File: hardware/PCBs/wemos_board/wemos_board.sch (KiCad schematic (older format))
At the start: 6 parts, among them J1 USB, J2 Servo, U1 WeMos_D1_mini

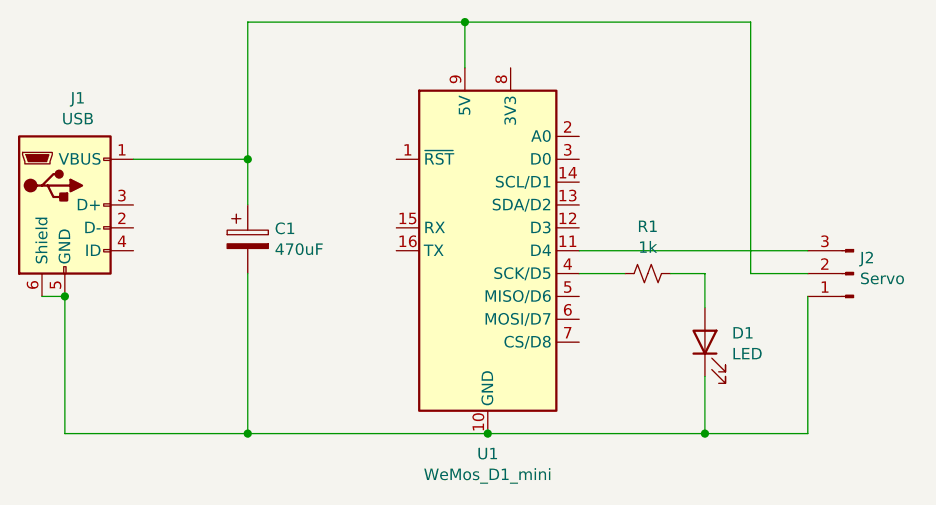
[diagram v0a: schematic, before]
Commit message: fix: wemos_board fix footprints and added rst control line
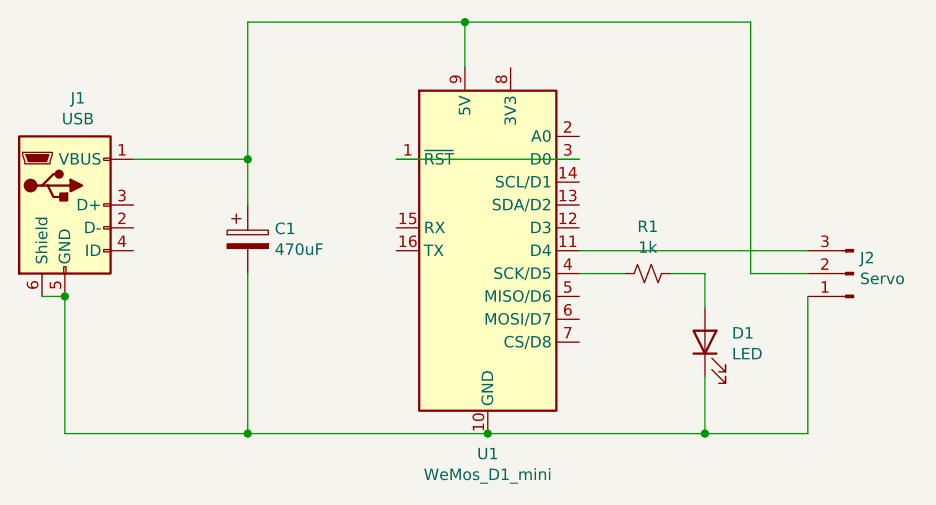
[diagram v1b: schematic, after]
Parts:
- J1: footprint Connector_USB:USB_Micro-B_Amphenol_10103594-0001LF_Horizontal -> Connector_USB:USB_Micro-B_Molex_47346-0001
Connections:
- net at U1.1 (~RST): now also U1.3 (D0)
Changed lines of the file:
@@
 F 0 "J1" H 3757 4467 50  0000 C CNN
 F 1 "USB" H 3757 4376 50  0000 C CNN
-F 2 "Connector_USB:USB_Micro-B_Amphenol_10103594-0001LF_Horizontal" H 3850 3950 50  0001 C CNN
+F 2 "Connector_USB:USB_Micro-B_Molex_47346-0001" H 3850 3950 50  0001 C CNN
 F 3 "~" H 3850 3950 50  0001 C CNN
 	1    3700 4000
@@
 	6700 3200 5450 3200
 Connection ~ 5450 3200
+Wire Wire Line
+	5950 3800 5150 3800
 $EndSCHEMATC
